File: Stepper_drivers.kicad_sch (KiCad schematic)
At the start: 27 parts, among them J10 Conn_01x06_Socket, J5 Conn_01x06_Socket, J6 Conn_01x06_Socket, J7 Conn_01x06_Socket, J8 Conn_01x06_Socket, J9 Conn_01x06_Socket, U12 HT26LS31ARZ, U13 HT26LS31ARZ, U14 HT26LS31ARZ, U3 ADuM1201AR, U4 ADuM1201AR, U5 ADuM1201AR, U6 ADuM1201AR, U7 ADuM1201AR, U8 ADuM1201AR

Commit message: Changed board spec from Nucleo F446RE to F446ZE Altered readme to suit it and moved the Todos over.
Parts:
- C10, C11, C12, C15, C23, C24, C4, C5, C6, C7, C8, C9: footprint (none) -> Capacitor_SMD:C_1206_3216Metric_Pad1.33x1.80mm_HandSolder
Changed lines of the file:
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@@
 			)
 		)
-		(property "Footprint" ""
+		(property "Footprint" "Capacitor_SMD:C_1206_3216Metric_Pad1.33x1.80mm_HandSolder"
 			(at 29.21 146.05 0)
 			(effects
@@
 			)
 		)
-		(property "Footprint" ""
+		(property "Footprint" "Capacitor_SMD:C_1206_3216Metric_Pad1.33x1.80mm_HandSolder"
 			(at 27.94 69.85 0)
 			(effects
@@
 			)
 		)
-		(property "Footprint" ""
+		(property "Footprint" "Capacitor_SMD:C_1206_3216Metric_Pad1.33x1.80mm_HandSolder"
 			(at 71.12 31.75 0)
 			(effects
@@
 			)
 		)
-		(property "Footprint" ""
+		(property "Footprint" "Capacitor_SMD:C_1206_3216Metric_Pad1.33x1.80mm_HandSolder"
 			(at 205.74 69.85 0)
 			(effects
@@
 			)
 		)
-		(property "Footprint" ""
+		(property "Footprint" "Capacitor_SMD:C_1206_3216Metric_Pad1.33x1.80mm_HandSolder"
 			(at 162.56 69.85 0)
 			(effects
@@
 			)
 		)
-		(property "Footprint" ""
+		(property "Footprint" "Capacitor_SMD:C_1206_3216Metric_Pad1.33x1.80mm_HandSolder"
 			(at 29.21 107.95 0)
 			(effects
@@
 			)
 		)
-		(property "Footprint" ""
+		(property "Footprint" "Capacitor_SMD:C_1206_3216Metric_Pad1.33x1.80mm_HandSolder"
 			(at 72.39 107.95 0)
 			(effects
@@
 			)
 		)
-		(property "Footprint" ""
+		(property "Footprint" "Capacitor_SMD:C_1206_3216Metric_Pad1.33x1.80mm_HandSolder"
 			(at 71.12 69.85 0)
 			(effects
@@
 			)
 		)
-		(property "Footprint" ""
+		(property "Footprint" "Capacitor_SMD:C_1206_3216Metric_Pad1.33x1.80mm_HandSolder"
 			(at 72.39 146.05 0)
 			(effects
@@
 			)
 		)
-		(property "Footprint" ""
+		(property "Footprint" "Capacitor_SMD:C_1206_3216Metric_Pad1.33x1.80mm_HandSolder"
 			(at 27.94 31.75 0)
 			(effects
@@
 			)
 		)
-		(property "Footprint" ""
+		(property "Footprint" "Capacitor_SMD:C_1206_3216Metric_Pad1.33x1.80mm_HandSolder"
 			(at 205.74 31.75 0)
 			(effects
@@
 			)
 		)
-		(property "Footprint" ""
+		(property "Footprint" "Capacitor_SMD:C_1206_3216Metric_Pad1.33x1.80mm_HandSolder"
 			(at 162.56 31.75 0)
 			(effects

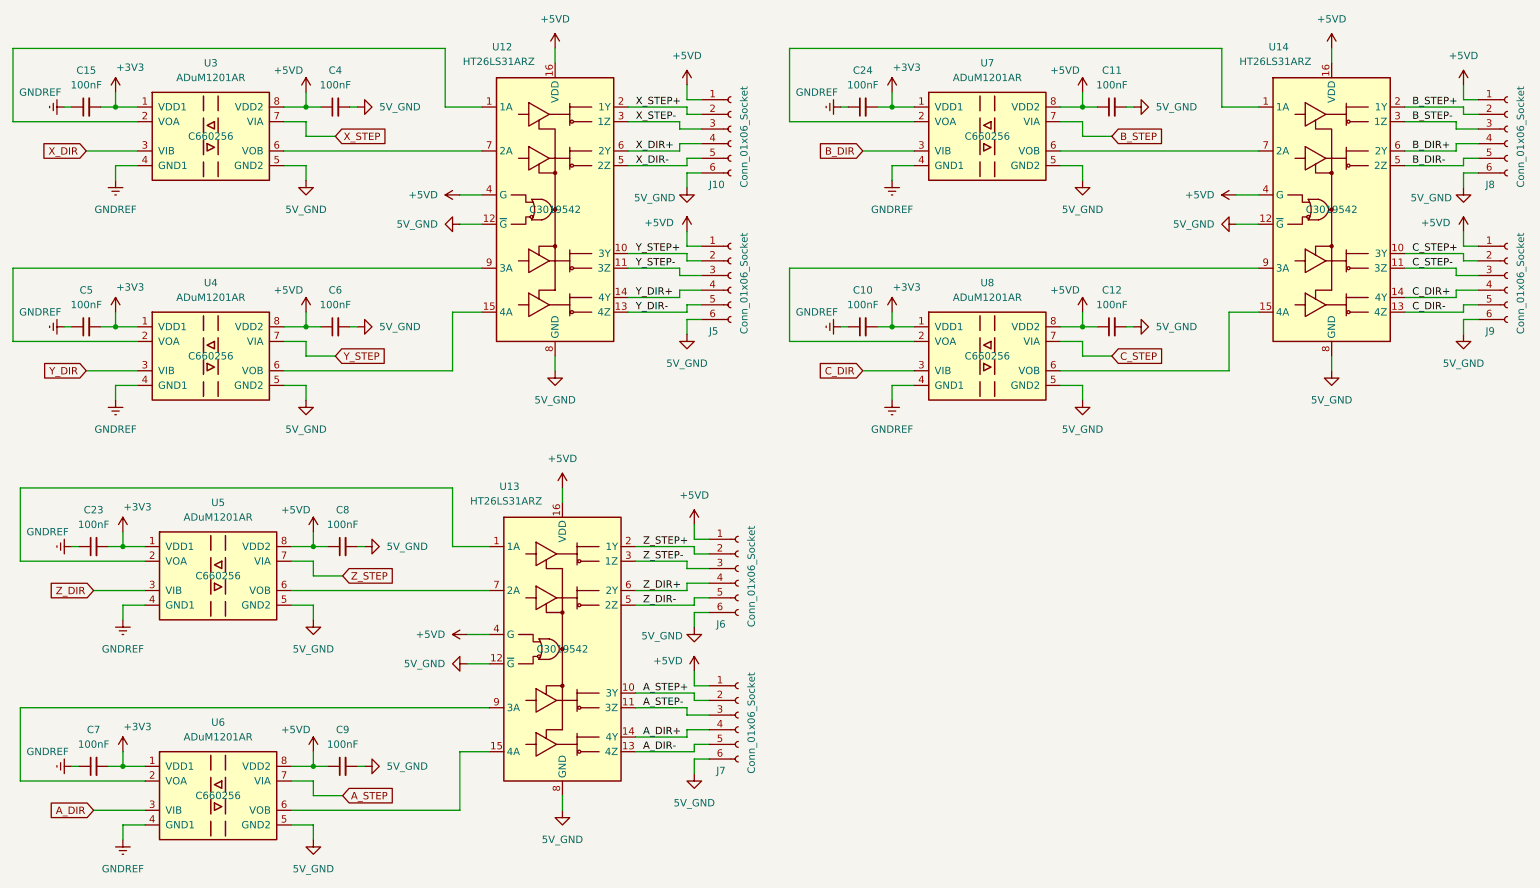
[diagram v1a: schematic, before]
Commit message: changes some unecessary global labels to local. Added a heirarchical sheet for output driver and basic numbering. Sink logic not yet set for O/Ps, but placeholder for now
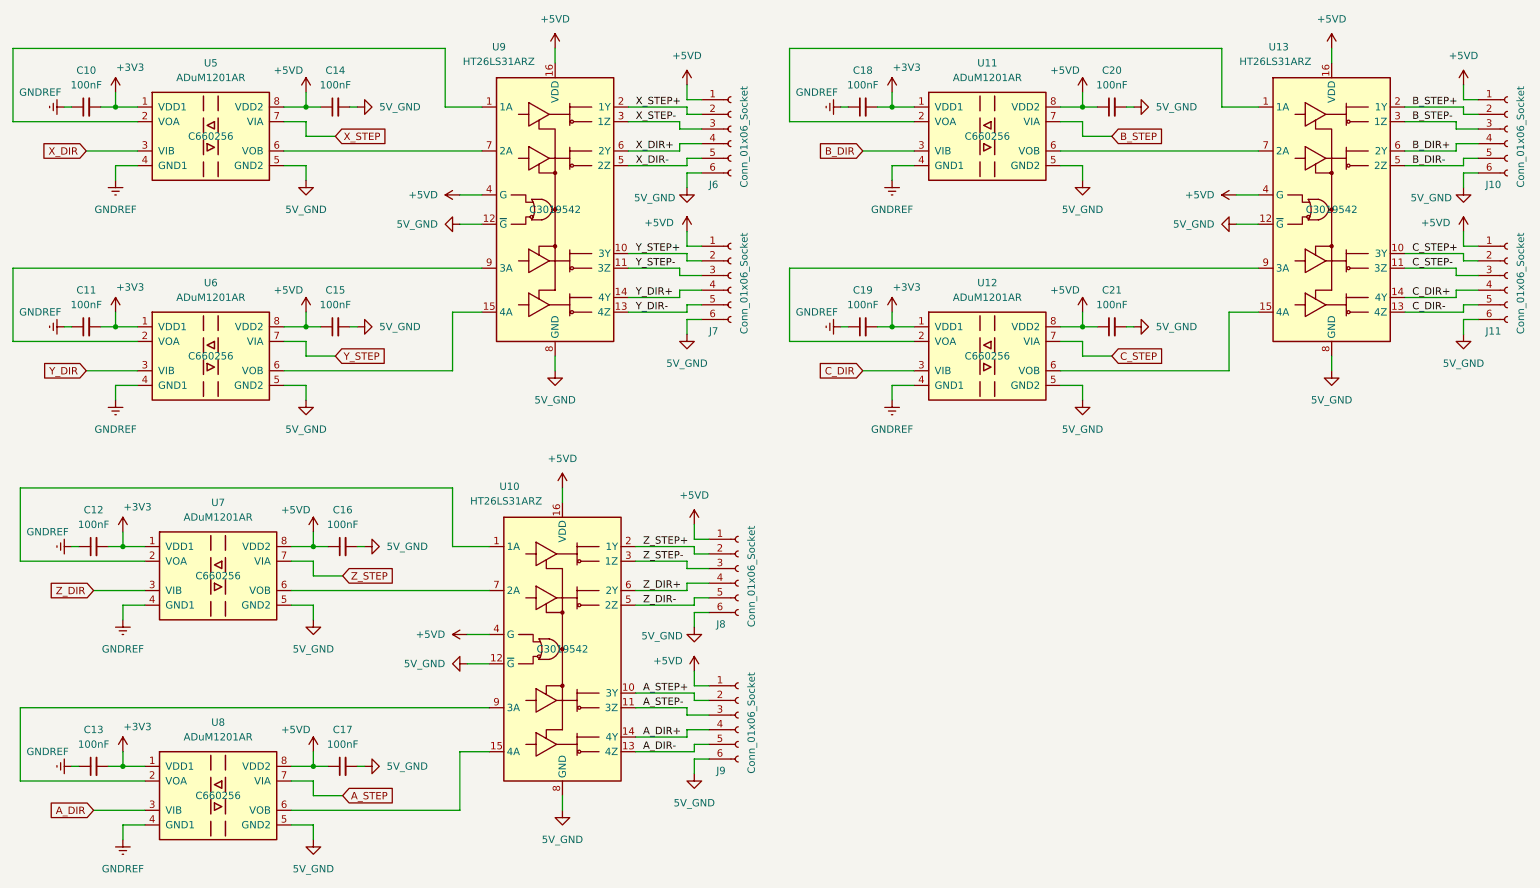
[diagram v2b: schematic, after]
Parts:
- renumbered C15 to C10, C5 to C11, C23 to C12, C7 to C13, C4 to C14, C6 to C15, C8 to C16, C9 to C17, C24 to C18, C10 to C19, C11 to C20, C12 to C21, J8 to J10, J9 to J11, J10 to J6, J5 to J7, J6 to J8, J7 to J9, U13 to U10, U7 to U11, U8 to U12, U14 to U13, U3 to U5, U4 to U6, U5 to U7, U6 to U8, U12 to U9

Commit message: redrew stepper drivers as duplicatable heirarchical sheets, moved jumpers into power managemente sheet, moved LEDs and user buttons into own sheet to save space. Fixed a few random labelling issues.
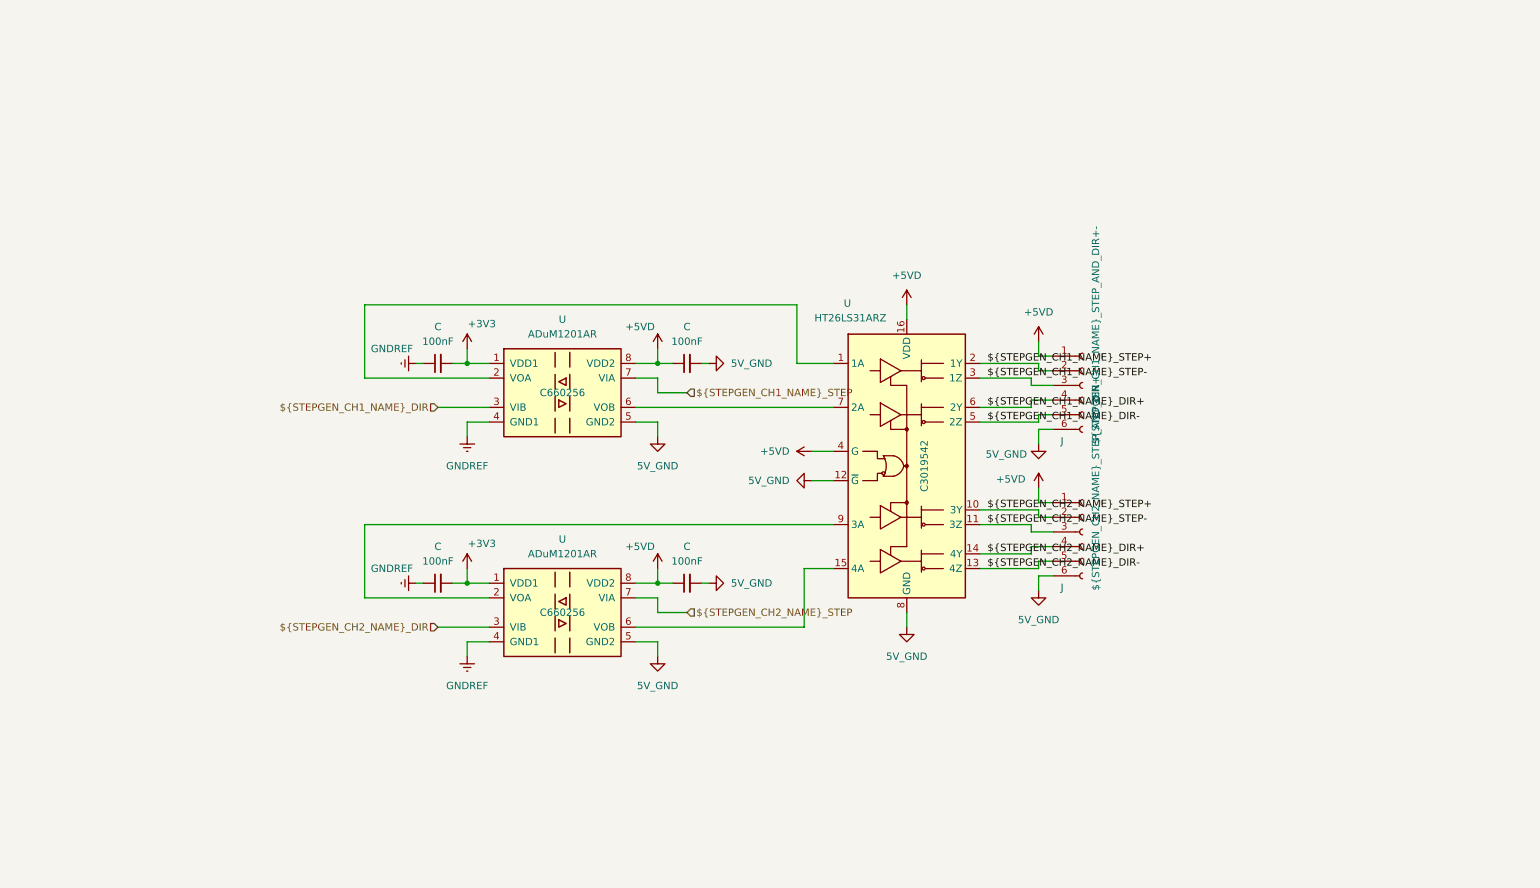
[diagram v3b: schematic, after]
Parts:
- removed C12, C13, C16, C17, C18, C19, C20, C21: 100nF, Capacitor_SMD:C_1206_3216Metric_Pad1.33x1.80mm_HandSolder, symbol Device:C_Small
- removed J10, J11, J8, J9: Conn_01x06_Socket, symbol Connector:Conn_01x06_Socket
- removed U10, U13: HT26LS31ARZ, Package_SO:SOIC-16_3.9x9.9mm_P1.27mm, symbol Interface:AM26LS31CD
- removed U11, U12, U7, U8: ADuM1201AR, Package_SO:SOIC-8_3.9x4.9mm_P1.27mm, symbol Isolator:ADuM1201AR
- J: renamed from J6; value Conn_01x06_Socket -> ${STEPGEN_CH1_NAME}_STEP_AND_DIR+-
- J: renamed from J7; value Conn_01x06_Socket -> ${STEPGEN_CH2_NAME}_STEP_AND_DIR+-
- renumbered C11 to C, C14 to C, C15 to C, C10 to C, U6 to U, U9 to U, U5 to U
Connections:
- net X_DIR renamed ${STEPGEN_CH1_NAME}_DIR
- net X_DIR+ renamed ${STEPGEN_CH1_NAME}_DIR+
- net X_DIR- renamed ${STEPGEN_CH1_NAME}_DIR-
- net X_STEP renamed ${STEPGEN_CH1_NAME}_STEP
- net X_STEP+ renamed ${STEPGEN_CH1_NAME}_STEP+
- net X_STEP- renamed ${STEPGEN_CH1_NAME}_STEP-
- net Y_DIR renamed ${STEPGEN_CH2_NAME}_DIR
- net Y_DIR+ renamed ${STEPGEN_CH2_NAME}_DIR+
- net Y_DIR- renamed ${STEPGEN_CH2_NAME}_DIR-
- net Y_STEP renamed ${STEPGEN_CH2_NAME}_STEP
- net Y_STEP+ renamed ${STEPGEN_CH2_NAME}_STEP+
- net Y_STEP- renamed ${STEPGEN_CH2_NAME}_STEP-
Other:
- moved on the sheet: C, J, U

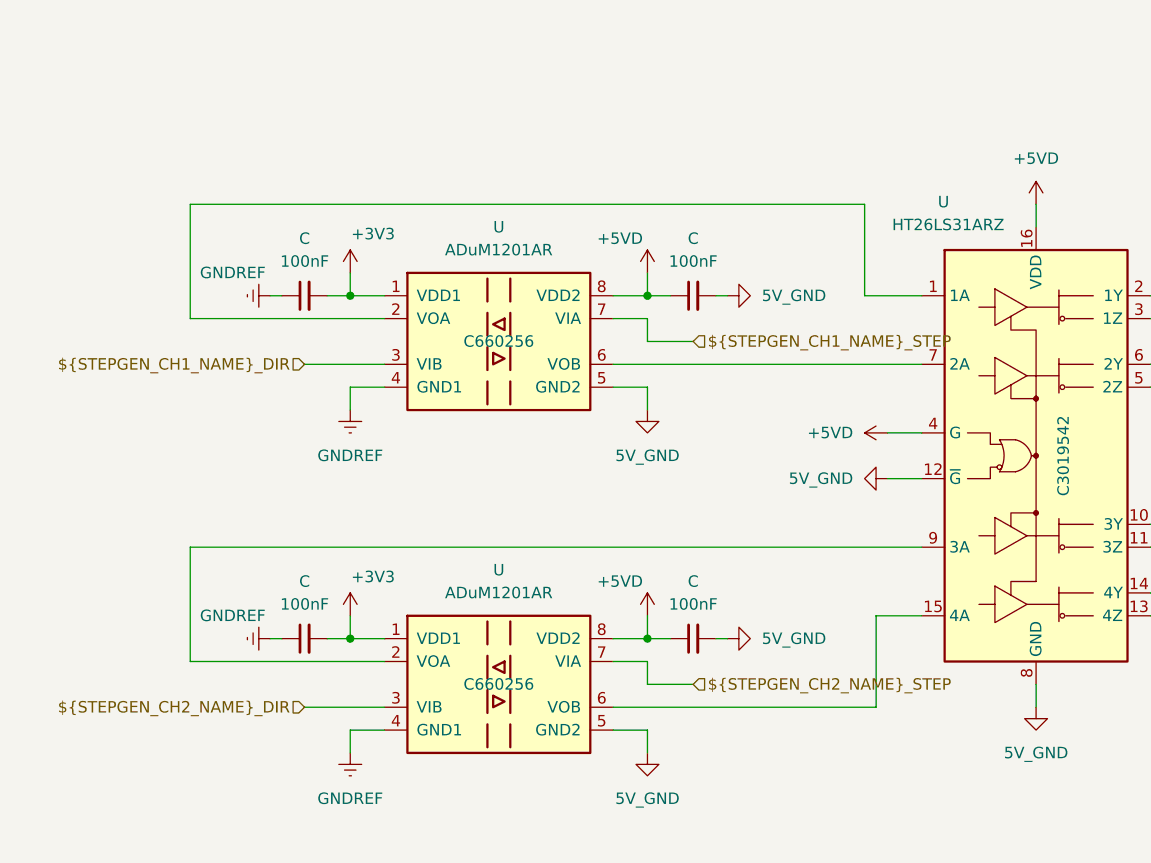
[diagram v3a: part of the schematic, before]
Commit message: Found a bug in the circuit, using the wrong isolated tranceivers, fixed.
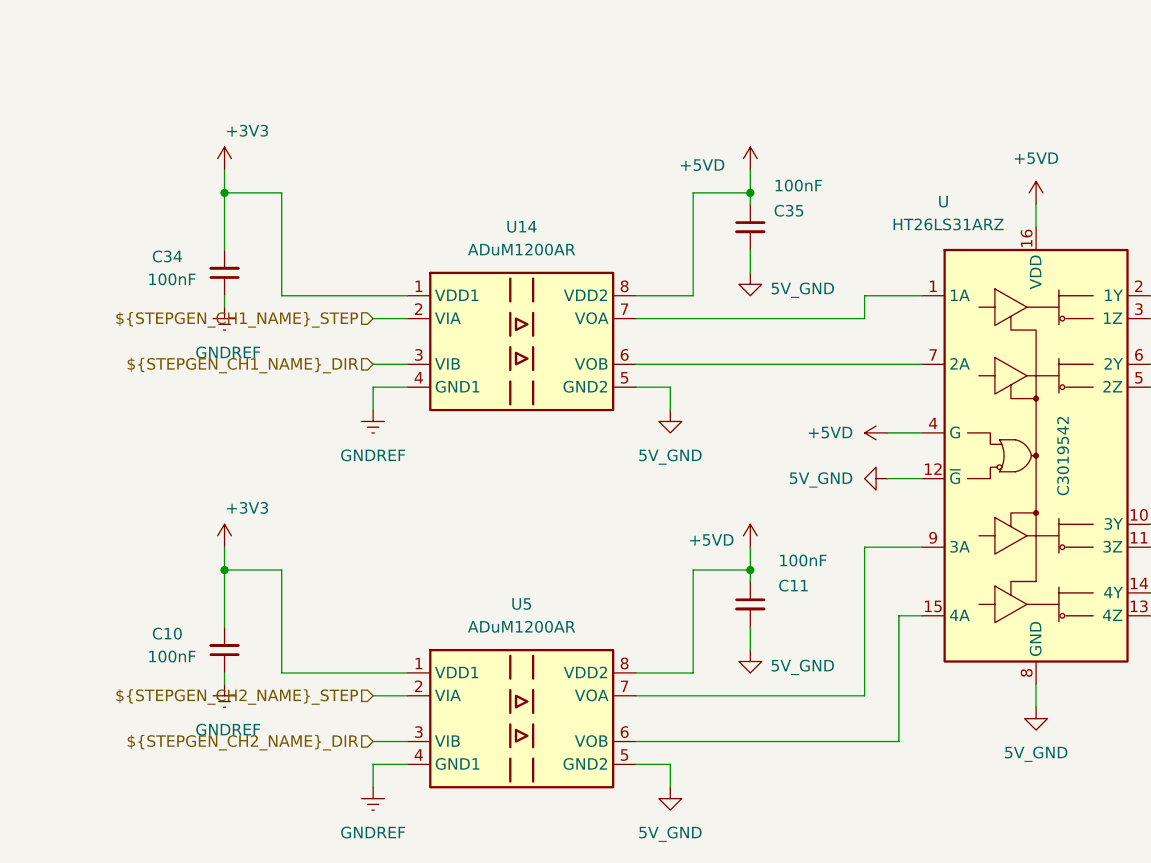
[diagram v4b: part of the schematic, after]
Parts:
- removed C (x4): 100nF, Capacitor_SMD:C_1206_3216Metric_Pad1.33x1.80mm_HandSolder, symbol Device:C_Small
- removed U (x2): ADuM1201AR, Package_SO:SOIC-8_3.9x4.9mm_P1.27mm, symbol Isolator:ADuM1201AR
- added C10, C11, C34, C35: 100nF, Capacitor_SMD:C_1206_3216Metric_Pad1.33x1.80mm_HandSolder, symbol Device:C_Small
- added U14, U5: ADuM1200AR, Package_SO:SOIC-8_3.9x4.9mm_P1.27mm, symbol Isolator:ADuM1200AR
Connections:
- net ${STEPGEN_CH1_NAME}_DIR: now also U14.3 (VIB)
- net ${STEPGEN_CH1_NAME}_STEP: now also U14.2 (VIA)
- net ${STEPGEN_CH2_NAME}_DIR: now also U5.3 (VIB)
- net ${STEPGEN_CH2_NAME}_STEP: now also U5.2 (VIA)
- net +3V3: now also C10.2, C34.2, U14.1 (VDD1), U5.1 (VDD1)
- net +5VD: now also C11.1, C35.1, U14.8 (VDD2), U5.8 (VDD2)
- net 5V_GND: now also C11.2, C35.2, U14.5 (GND2), U5.5 (GND2)
- net GNDREF: now also C10.1, C34.1, U14.4 (GND1), U5.4 (GND1)
- net at U.9 (3A): now also U5.7 (VOA)
- net at U.15 (4A): now also U5.6 (VOB)
- net at U.1 (1A): now also U14.7 (VOA)
- net at U.7 (2A): now also U14.6 (VOB)

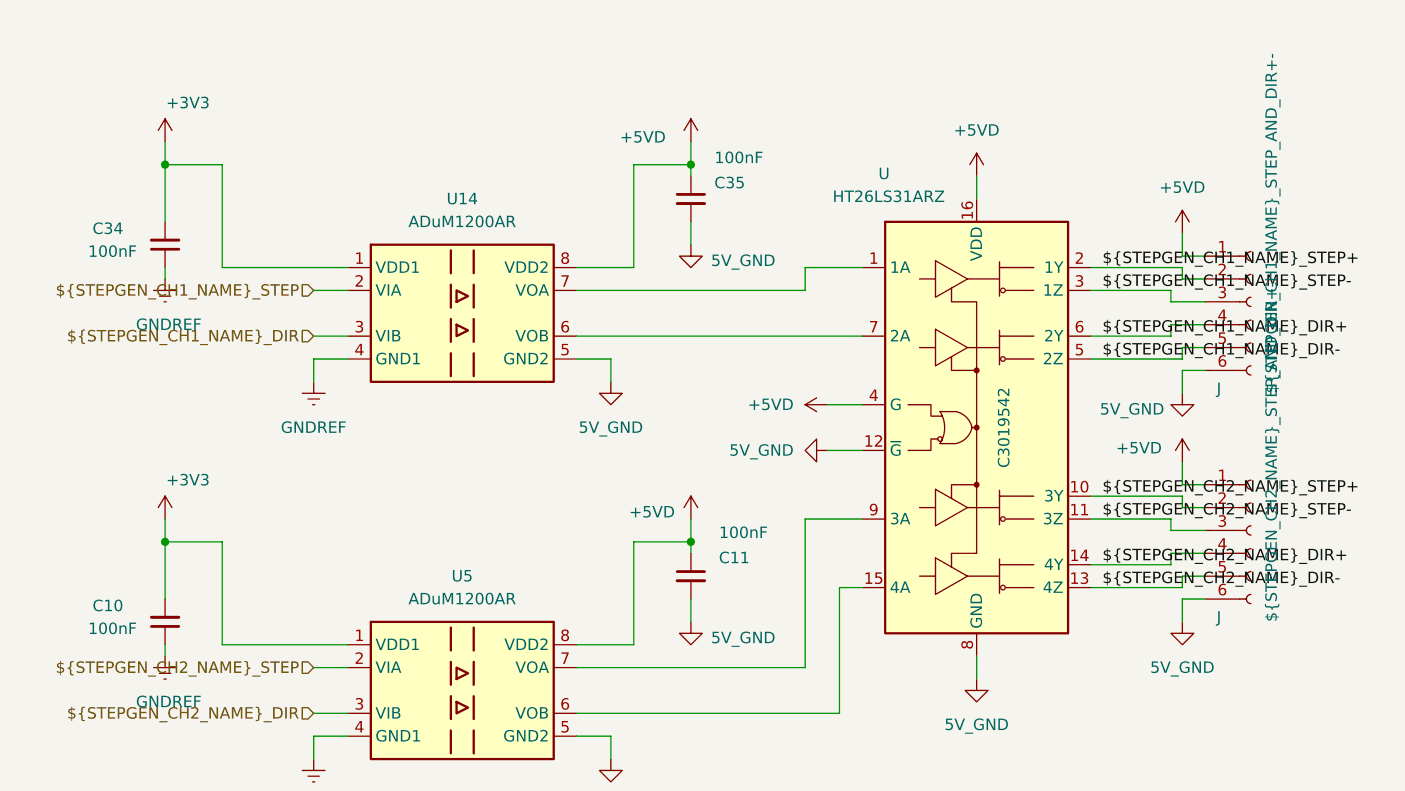
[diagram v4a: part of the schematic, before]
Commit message: Completed design for digital outputs, tidied into own sheets and bussing for scalability
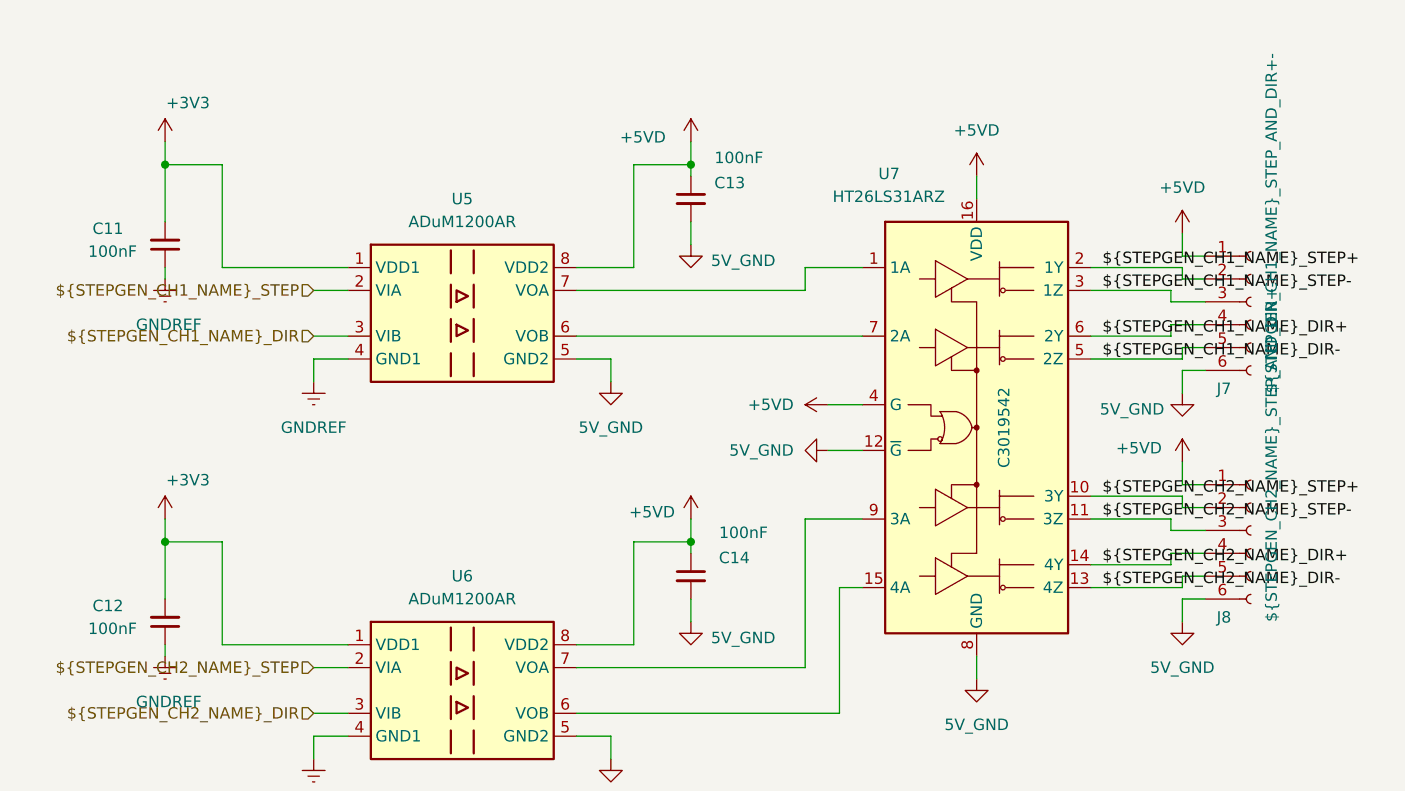
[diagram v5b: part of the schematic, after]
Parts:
- renumbered C34 to C11, C10 to C12, C35 to C13, C11 to C14, J to J7, J to J8, U14 to U5, U5 to U6, U to U7
